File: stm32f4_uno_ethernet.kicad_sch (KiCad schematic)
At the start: 11 parts, among them J101 STM32 GPIO, J102 Digital/PWM, J103 STM32 GPIO, J104 STM32 GPIO, J105 STM32 GPIO, J106 Power, J107 Ethernet, J108 STM32 GPIO, J109 Digital/PWM, J110 Analog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

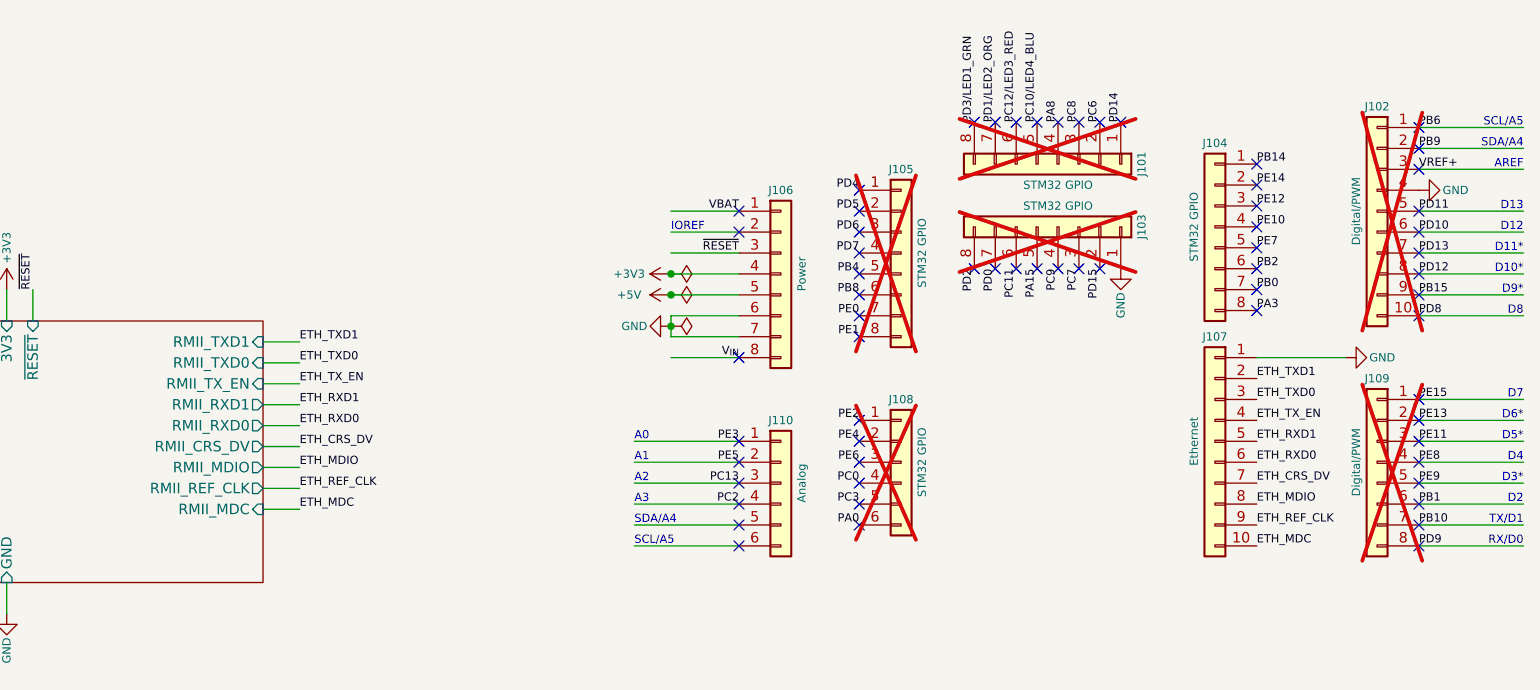
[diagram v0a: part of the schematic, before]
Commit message: Add ETH_RXER
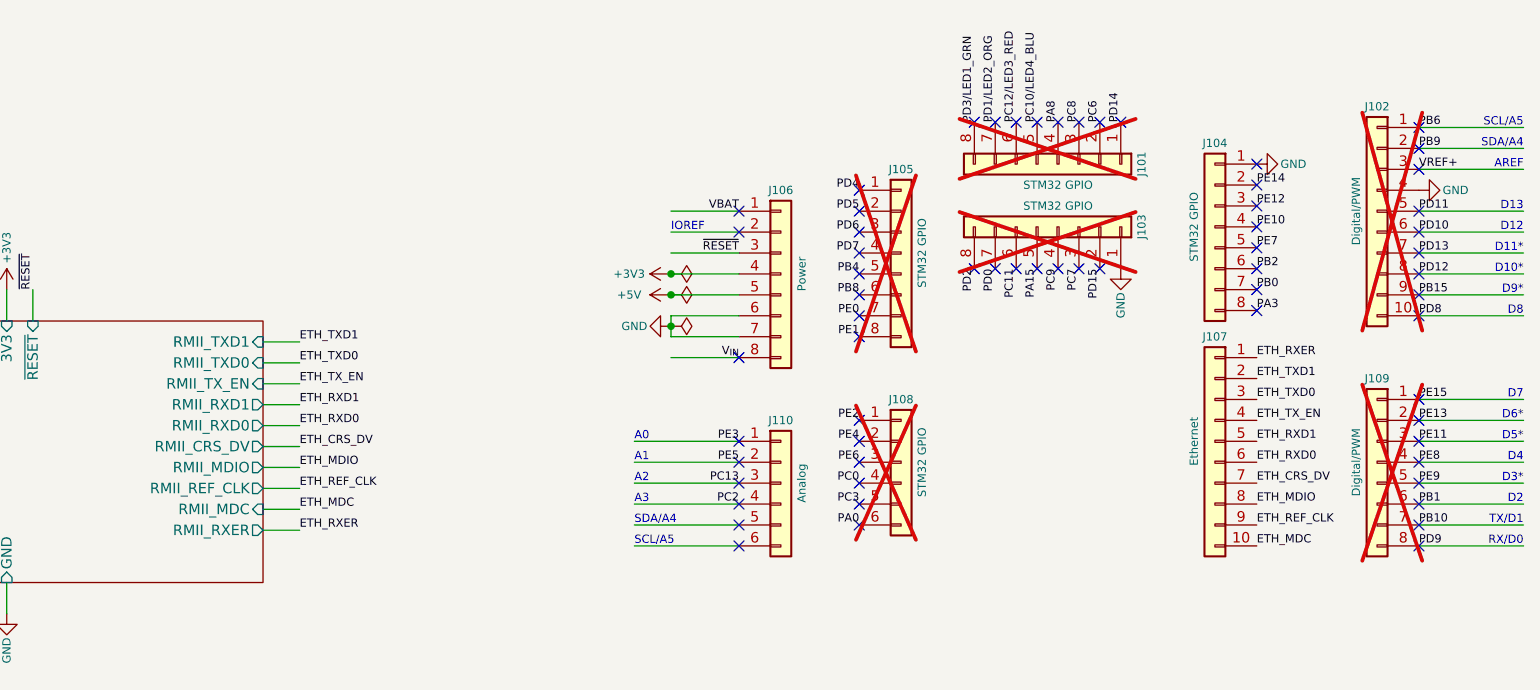
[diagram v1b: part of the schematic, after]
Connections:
- net PB14 is gone; now on net GND: J104.1 (Pin_1)
- net GND: no longer J107.1 (Pin_1)
- new net ETH_RXER: J107.1 (Pin_1)
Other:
- sheet Ethernet ports: added RMII_RXER; removed none

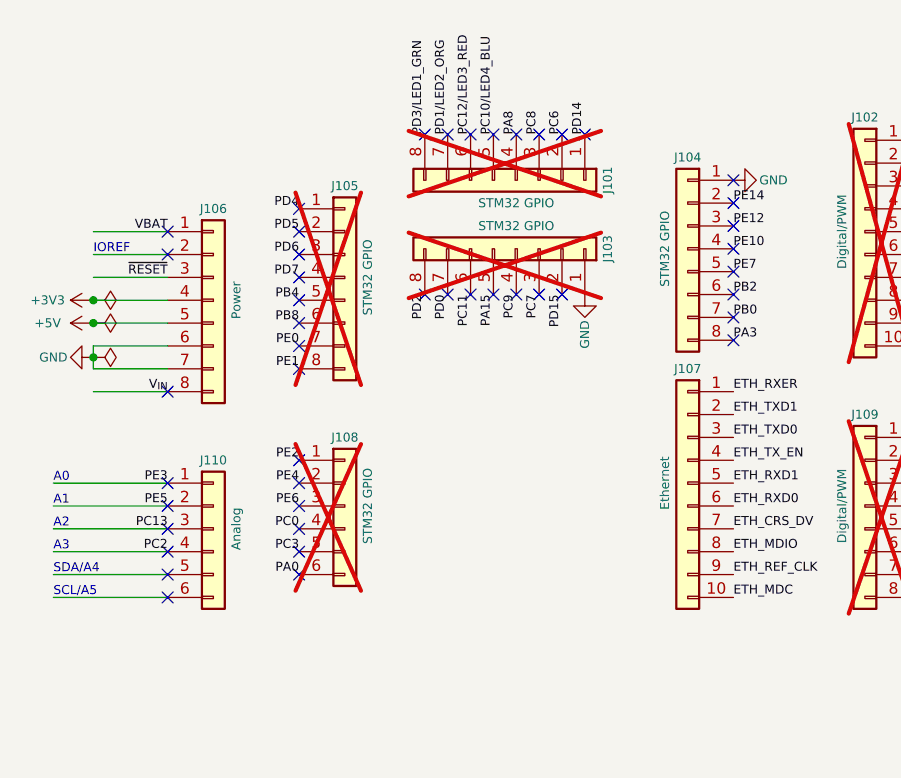
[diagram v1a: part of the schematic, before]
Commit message: Set DNP
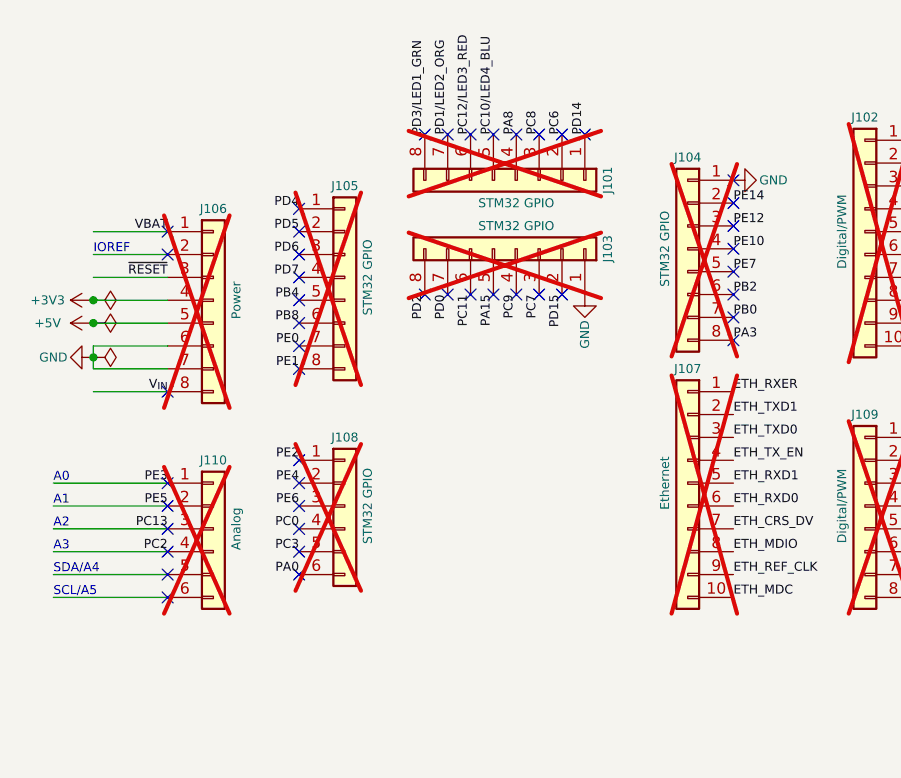
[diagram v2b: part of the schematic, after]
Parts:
- J104, J106, J107, J110: now not fitted; now left out of the parts list
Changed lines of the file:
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@@
   )
   (symbol (lib_id "Connector_Generic:Conn_01x08") (at 189.865 45.085 0) (unit 1)
-    (in_bom yes) (on_board yes) (dnp no)
+    (in_bom no) (on_board yes) (dnp yes)
     (property "Reference" "J106" (at 189.865 34.925 0)
       (effects (font (size 1 1)))
@@
     (property "Datasheet" "" (at 189.865 45.085 0)
       (effects (font (size 1 1)))
+    )
+    (property "Description" "" (at 189.865 45.085 0)
+      (effects (font (size 1.27 1.27)) hide)
+    )
+    (property "Manufacturer" "" (at 189.865 45.085 0)
+      (effects (font (size 1.27 1.27)) hide)
+    )
+    (property "Partnumber" "" (at 189.865 45.085 0)
+      (effects (font (size 1.27 1.27)) hide)
+    )
+    (property "JLCPCB Part #" "" (at 189.865 45.085 0)
+      (effects (font (size 1.27 1.27)) hide)
+    )
+    (property "isBasicPart" "" (at 189.865 45.085 0)
+      (effects (font (size 1.27 1.27)) hide)
+    )
+    (property "Description" "" (at 189.865 45.085 0)
+      (effects (font (size 1.27 1.27)) hide)
+    )
+    (property "Manufacturer" "" (at 189.865 45.085 0)
+      (effects (font (size 1.27 1.27)) hide)
+    )
+    (property "Partnumber" "" (at 189.865 45.085 0)
+      (effects (font (size 1.27 1.27)) hide)
+    )
+    (property "JLCPCB Part #" "" (at 189.865 45.085 0)
+      (effects (font (size 1.27 1.27)) hide)
+    )
+    (property "isBasicPart" "" (at 189.865 45.085 0)
+      (effects (font (size 1.27 1.27)) hide)
     )
     (pin "1")
@@
   )
   (symbol (lib_id "Connector_Generic:Conn_01x06") (at 189.865 70.485 0) (unit 1)
-    (in_bom yes) (on_board yes) (dnp no)
+    (in_bom no) (on_board yes) (dnp yes)
     (property "Reference" "J110" (at 189.865 62.865 0)
       (effects (font (size 1 1)))
@@
     (property "Datasheet" "~" (at 189.865 70.485 0)
       (effects (font (size 1 1)) hide)
+    )
+    (property "Description" "" (at 189.865 70.485 0)
+      (effects (font (size 1.27 1.27)) hide)
+    )
+    (property "Manufacturer" "" (at 189.865 70.485 0)
+      (effects (font (size 1.27 1.27)) hide)
+    )
+    (property "Partnumber" "" (at 189.865 70.485 0)
+      (effects (font (size 1.27 1.27)) hide)
+    )
+    (property "JLCPCB Part #" "" (at 189.865 70.485 0)
+      (effects (font (size 1.27 1.27)) hide)
+    )
+    (property "isBasicPart" "" (at 189.865 70.485 0)
+      (effects (font (size 1.27 1.27)) hide)
+    )
+    (property "Description" "" (at 189.865 70.485 0)
+      (effects (font (size 1.27 1.27)) hide)
+    )
+    (property "Manufacturer" "" (at 189.865 70.485 0)
+      (effects (font (size 1.27 1.27)) hide)
+    )
+    (property "Partnumber" "" (at 189.865 70.485 0)
+      (effects (font (size 1.27 1.27)) hide)
+    )
+    (property "JLCPCB Part #" "" (at 189.865 70.485 0)
+      (effects (font (size 1.27 1.27)) hide)
+    )
+    (property "isBasicPart" "" (at 189.865 70.485 0)
+      (effects (font (size 1.27 1.27)) hide)
     )
     (pin "1")
@@
   )
   (symbol (lib_id "Connector_Generic:Conn_01x10") (at 242.57 65.405 0) (mirror y) (unit 1)
-    (in_bom yes) (on_board yes) (dnp no)
+    (in_bom no) (on_board yes) (dnp yes)
     (property "Reference" "J107" (at 242.57 52.705 0)
       (effects (font (size 1 1)))
@@
   )
   (symbol (lib_id "Connector_Generic:Conn_01x08") (at 242.57 39.37 0) (mirror y) (unit 1)
-    (in_bom yes) (on_board yes) (dnp no)
+    (in_bom no) (on_board yes) (dnp yes)
     (property "Reference" "J104" (at 242.57 29.21 0)
       (effects (font (size 1 1)))
@@
       (effects (font (size 1 1)))
     )
-    (pin "1")
+    (property "Description" "" (at 242.57 39.37 0)
+      (effects (font (size 1.27 1.27)) hide)
+    )
+    (property "Manufacturer" "" (at 242.57 39.37 0)
+      (effects (font (size 1.27 1.27)) hide)
+    )
+    (property "Partnumber" "" (at 242.57 39.37 0)
+      (effects (font (size 1.27 1.27)) hide)
+    )
+    (property "JLCPCB Part #" "" (at 242.57 39.37 0)
+      (effects (font (size 1.27 1.27)) hide)
+    )
+    (property "isBasicPart" "" (at 242.57 39.37 0)
+      (effects (font (size 1.27 1.27)) hide)
+    )
+    (property "Description" "" (at 242.57 39.37 0)
+      (effects (font (size 1.27 1.27)) hide)
+    )
+    (property "Manufacturer" "" (at 242.57 39.37 0)
+      (effects (font (size 1.27 1.27)) hide)
+    )
+    (property "Partnumber" "" (at 242.57 39.37 0)
+      (effects (font (size 1.27 1.27)) hide)
+    )
+    (property "JLCPCB Part #" "" (at 242.57 39.37 0)
+      (effects (font (size 1.27 1.27)) hide)
+    )
+    (property "isBasicPart" "" (at 242.57 39.37 0)
+      (effects (font (size 1.27 1.27)) hide)
+    )
+    (pin "1")

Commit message: #1 Use new central library KiCad-Lib
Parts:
- J106, J107: now fitted
- J111: now left out of the parts list
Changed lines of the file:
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@@
   )
   (symbol (lib_id "Connector_Generic:Conn_01x08") (at 189.865 45.085 0) (unit 1)
-    (in_bom no) (on_board yes) (dnp yes)
+    (in_bom no) (on_board yes) (dnp no)
     (property "Reference" "J106" (at 189.865 34.925 0)
       (effects (font (size 1 1)))
@@
   )
   (symbol (lib_id "Connector_Generic:Conn_01x10") (at 242.57 65.405 0) (mirror y) (unit 1)
-    (in_bom no) (on_board yes) (dnp yes)
+    (in_bom no) (on_board yes) (dnp no)
     (property "Reference" "J107" (at 242.57 52.705 0)
       (effects (font (size 1 1)))
@@
   )
   (symbol (lib_id "Connector_Generic:Conn_01x04") (at 54.61 59.69 0) (mirror y) (unit 1)
-    (in_bom yes) (on_board yes) (dnp no) (fields_autoplaced)
+    (in_bom no) (on_board yes) (dnp no) (fields_autoplaced)
     (property "Reference" "J111" (at 54.61 50.8 0)
       (effects (font (size 1 1)))

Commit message: #2 Add silkscreen texts
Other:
- company: (none) -> easy-smart solution GmbH
- title: (none) -> STM32F4 Uno Ethernet
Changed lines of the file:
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@@
   (paper "A4")
   (title_block
-    (date "mar. 31 mars 2015")
+    (title "STM32F4 Uno Ethernet")
+    (date "2023-10-02")
+    (rev "1.0.x-dev")
+    (company "easy-smart solution GmbH")
   )
   (junction (at 176.53 45.085) (diameter 0) (color 0 0 0 0)
